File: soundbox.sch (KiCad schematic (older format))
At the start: 9 parts, among them J1 MICRO_SD_CARD_HOLDER

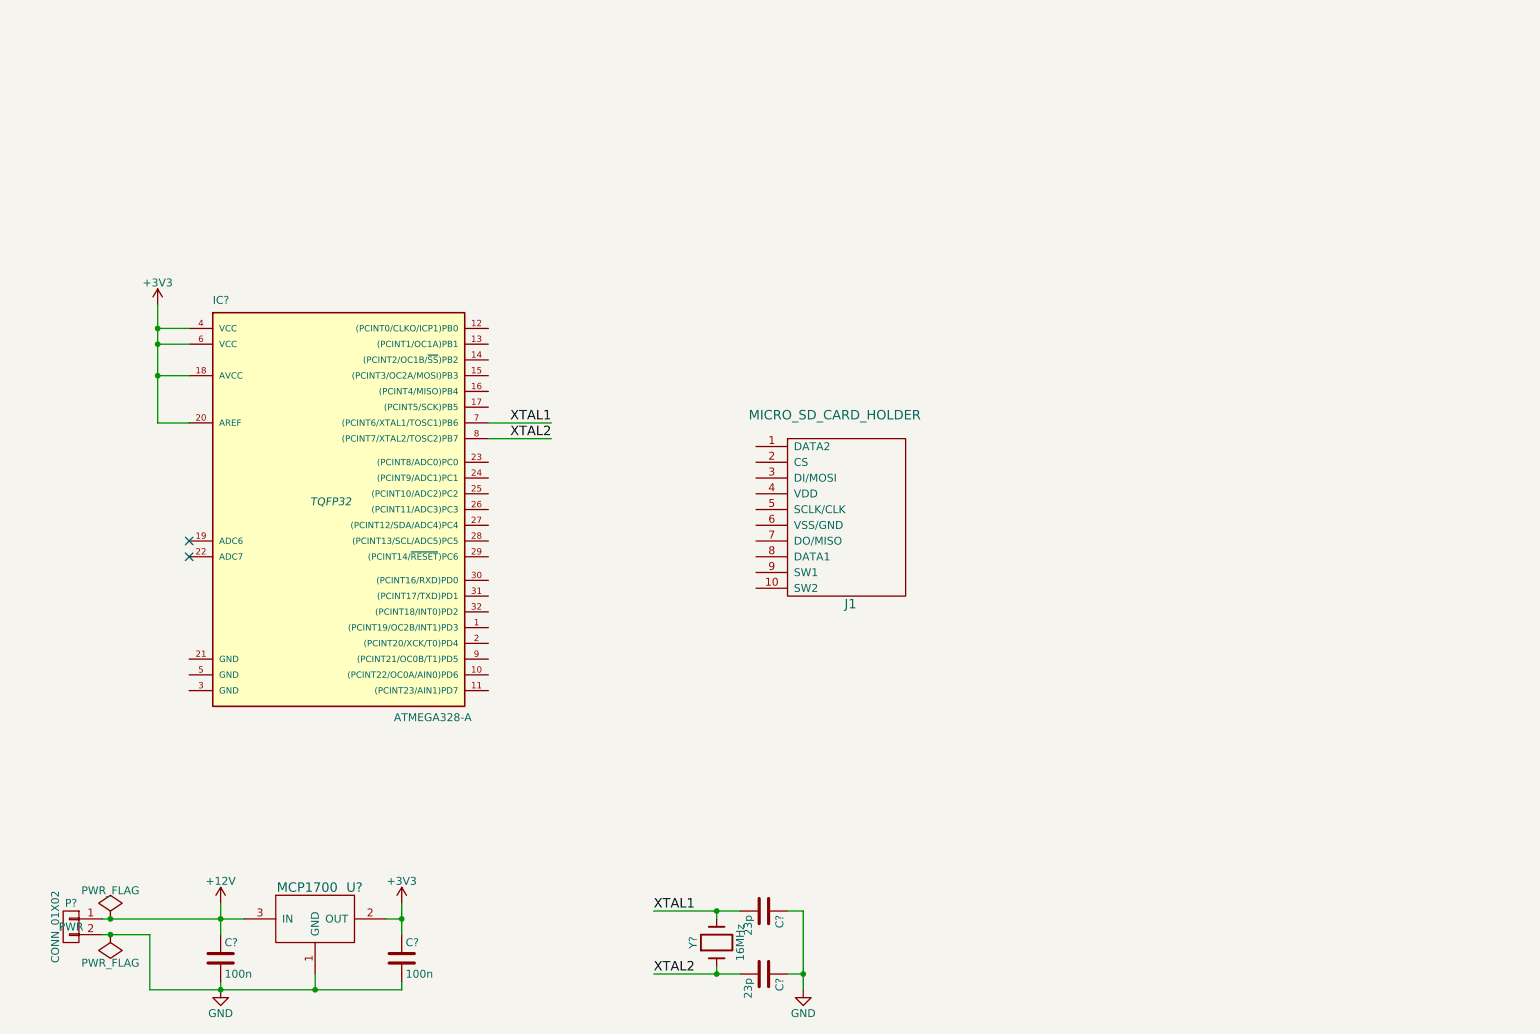
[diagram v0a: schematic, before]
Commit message: final version of schematic packages assigned raw placement on layout
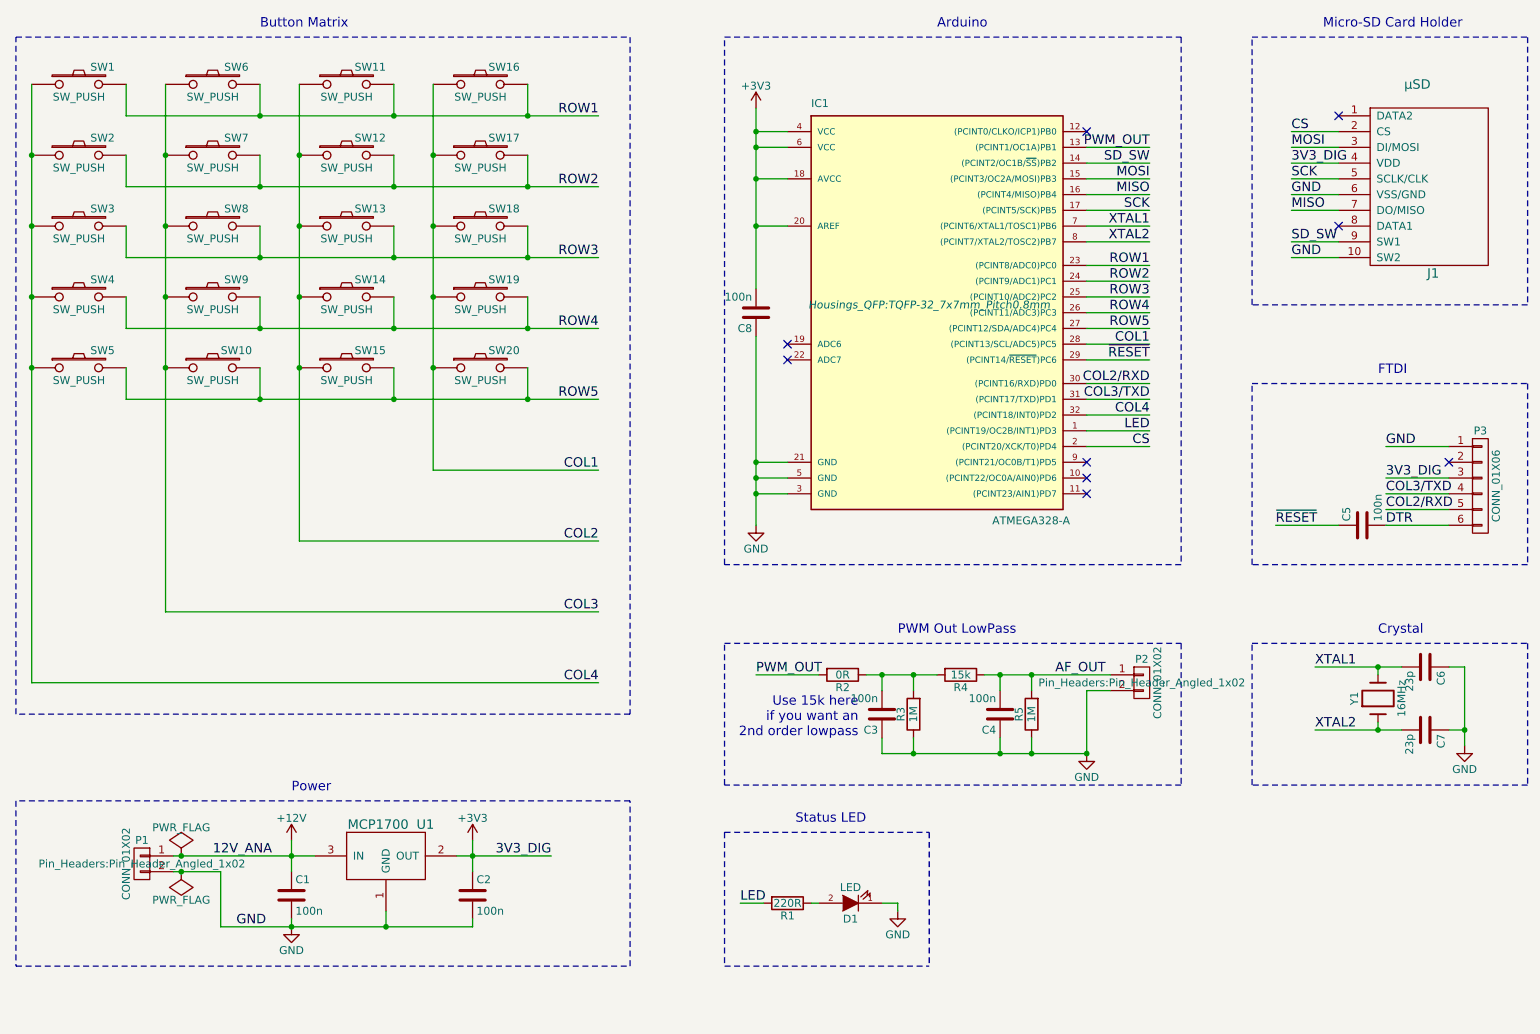
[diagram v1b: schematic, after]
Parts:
- added C3, C4, C5, C8: 100n, Capacitors_SMD:C_0603, symbol C
- added D1: LED, led:led-CHIPLED_0603, symbol LED
- added P2: CONN_01X02, Pin_Headers:Pin_Header_Angled_1x02, symbol CONN_01X02
- added P3: CONN_01X06, Pin_Headers:Pin_Header_Angled_1x06, symbol CONN_01X06
- added R1: 220R, Resistors_SMD:R_0603, symbol R
- added R2: 0R, Resistors_SMD:R_0603, symbol R
- added R3, R5: 1M, Resistors_SMD:R_0603, symbol R
- added R4: 15k, Resistors_SMD:R_0603, symbol R
- added SW1, SW10, SW11, SW12, SW13, SW14, SW15, SW16, SW17, SW18, SW19, SW2, SW20, SW3, SW4, SW5, SW6, SW7, SW8, SW9: SW_PUSH, Buttons_Switches_SMD:SW_SPST_PTS645, symbol SW_PUSH
- C1, C2, C6, C7: renamed from C?; footprint (none) -> Capacitors_SMD:C_0603
- IC1: renamed from IC?; footprint TQFP32 -> Housings_QFP:TQFP-32_7x7mm_Pitch0.8mm
- J1: value MICRO_SD_CARD_HOLDER -> µSD
- P1: renamed from P?; footprint PWR -> Pin_Headers:Pin_Header_Angled_1x02
- U1: renamed from U?; footprint (none) -> TO_SOT_Packages_SMD:SOT-23_Handsoldering
- Y1: renamed from Y?; footprint (none) -> Crystals:Crystal_HC49-SD_SMD
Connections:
- net +3V3: now also J1.4 (VDD), C8.2, P3.3 (P3)
- net GND: now also IC1.21 (GND), IC1.3 (GND), IC1.5 (GND), J1.10 (SW2), J1.6 (VSS/GND), C3.1, C4.1, C8.1, D1.1 (K), P2.2 (P2), P3.1 (P1), R3.1, R5.1
- net CS: now reaches J1.2 (CS)
- net CS: now also IC1.2 ((PCINT20/XCK/T0)PD4)
- net MOSI: now reaches J1.3 (DI/MOSI)
- net MOSI: now also IC1.15 ((PCINT3/OC2A/MOSI)PB3)
- net SCK: now reaches J1.5 (SCLK/CLK)
- net SCK: now also IC1.17 ((PCINT5/SCK)PB5)
- net MISO: now reaches J1.7 (DO/MISO)
- net MISO: now also IC1.16 ((PCINT4/MISO)PB4)
- net SD_SW: now reaches J1.9 (SW1)
- net SD_SW: now also IC1.14 ((PCINT2/OC1B/~SS~)PB2)
- net LED: now reaches IC1.1 ((PCINT19/OC2B/INT1)PD3)
- net LED: now also R1.2
- net PWM_OUT: now reaches IC1.13 ((PCINT1/OC1A)PB1)
- net PWM_OUT: now also R2.2
- net ROW1: now reaches IC1.23 ((PCINT8/ADC0)PC0)
- net ROW1: now also SW1.2, SW11.2, SW16.2, SW6.2
- net ROW2: now reaches IC1.24 ((PCINT9/ADC1)PC1)
- net ROW2: now also SW12.2, SW17.2, SW2.2, SW7.2
- net ROW3: now reaches IC1.25 ((PCINT10/ADC2)PC2)
- net ROW3: now also SW13.2, SW18.2, SW3.2, SW8.2
- net ROW4: now reaches IC1.26 ((PCINT11/ADC3)PC3)
- net ROW4: now also SW14.2, SW19.2, SW4.2, SW9.2
- net ROW5: now reaches IC1.27 ((PCINT12/SDA/ADC4)PC4)
- net ROW5: now also SW10.2, SW15.2, SW20.2, SW5.2
- net COL1: now reaches IC1.28 ((PCINT13/SCL/ADC5)PC5)
- net COL1: now also SW16.1, SW17.1, SW18.1, SW19.1, SW20.1
- net ~RESET: now reaches IC1.29 ((PCINT14/~RESET~)PC6)
- net ~RESET: now also C5.1
- net COL2/RXD: now reaches IC1.30 ((PCINT16/RXD)PD0)
- net COL2/RXD: now also P3.5 (P5)
- net COL3/TXD: now reaches IC1.31 ((PCINT17/TXD)PD1)
- net COL3/TXD: now also P3.4 (P4)
- net COL4: now reaches IC1.32 ((PCINT18/INT0)PD2)
- net COL4: now also SW1.1, SW2.1, SW3.1, SW4.1, SW5.1
- new net: C3.2, R2.1, R3.2, R4.2
- new net: D1.2 (A), R1.1
- new net AF_OUT: C4.2, P2.1 (P1), R4.1, R5.2
- new net COL2: SW11.1, SW12.1, SW13.1, SW14.1, SW15.1
- new net COL3: SW10.1, SW6.1, SW7.1, SW8.1, SW9.1
- new net DTR: C5.2, P3.6 (P6)
- no-connect marks 2 -> 9
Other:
- note added: "Arduino"
- note added: "Button Matrix"
- note added: "Crystal"
- note added: "FTDI"
- note added: "Micro-SD Card Holder"
- note added: "PWM Out LowPass"
- note added: "Power"
- note added: "Status LED"
- note added: "Use 15k here\nif you want an\n2nd order lowpass"
- moved on the sheet: C1, C2, C6, C7, IC1, J1, P1, U1, Y1
